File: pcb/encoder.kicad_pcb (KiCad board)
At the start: 2 copper layers, 32 x 57 mm, 2 parts, among them SW1 RKJXT1F42001, U1 Xiao2040

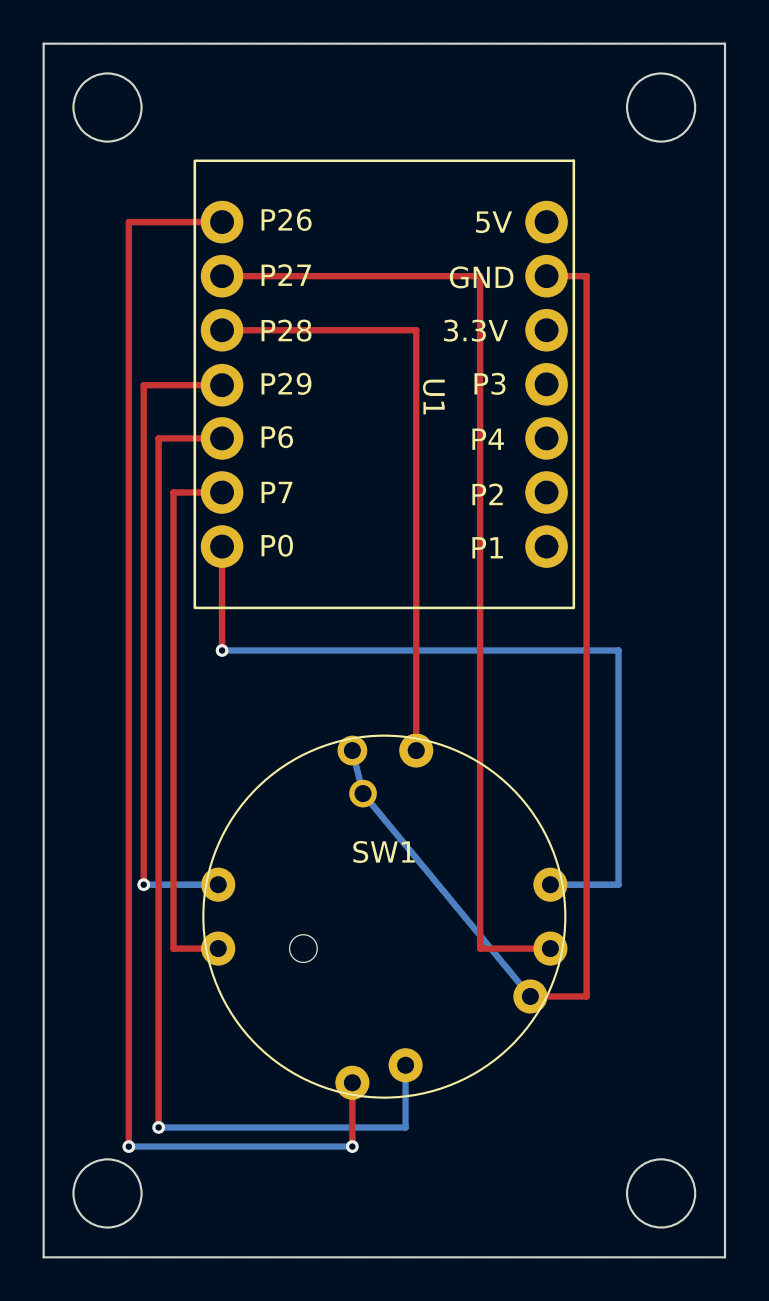
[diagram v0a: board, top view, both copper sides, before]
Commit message: Update PCB to bottom-layer-only routing constraints
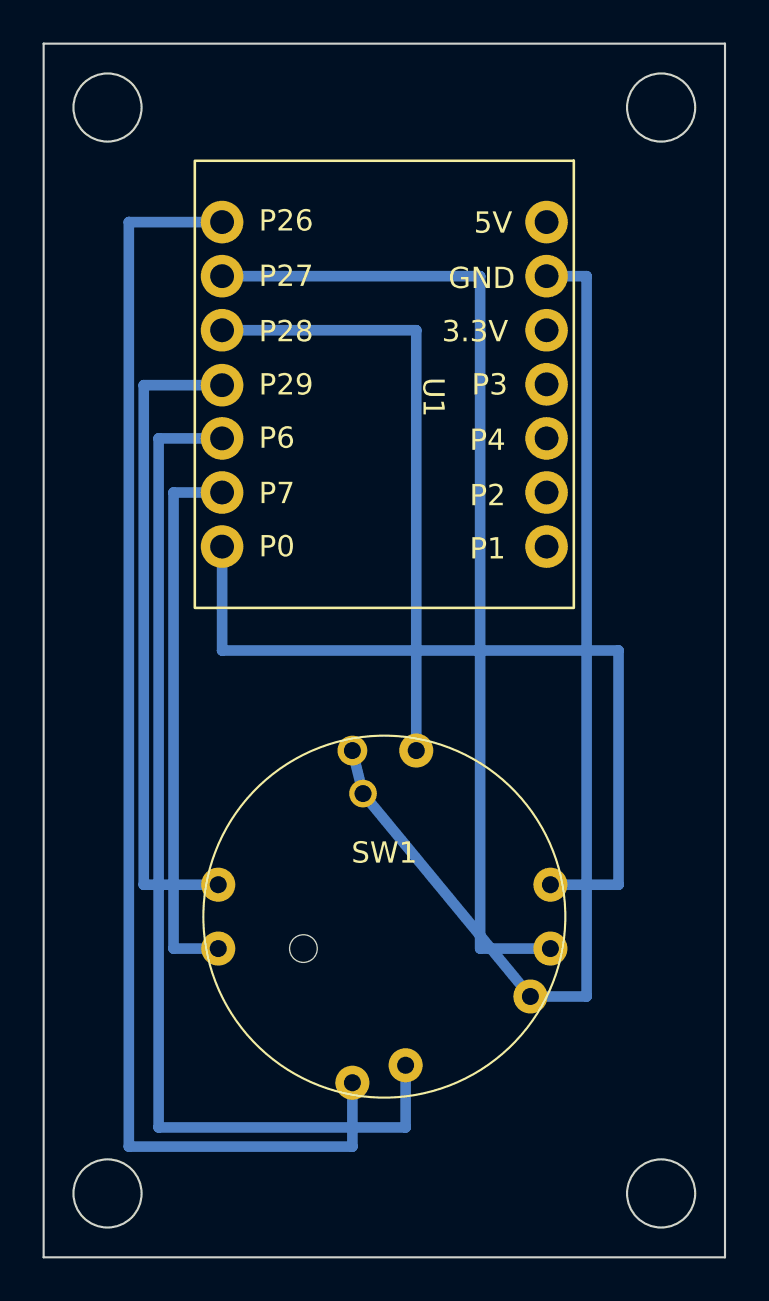
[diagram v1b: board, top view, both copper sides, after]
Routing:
- net SW_PUSH: vias 1 -> 0
- net SW_D: vias 1 -> 0
- net SW_A: vias 2 -> 0
- net ENC_B: vias 1 -> 0
- removed copper zone on B.Cu, net GND
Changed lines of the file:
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@@
 		(start 109.5 103.75)
 		(end 106.86 103.75)
-		(width 0.3)
-		(layer "F.Cu")
+		(width 0.5)
+		(layer "B.Cu")
 		(net "GND")
 	)
@@
 		(start 109.5 69.92)
 		(end 109.5 103.75)
-		(width 0.3)
-		(layer "F.Cu")
+		(width 0.5)
+		(layer "B.Cu")
 		(net "GND")
 	)
@@
 		(start 107.62 69.92)
 		(end 109.5 69.92)
-		(width 0.3)
-		(layer "F.Cu")
+		(width 0.5)
+		(layer "B.Cu")
 		(net "GND")
 	)
@@
 		(start 99 94.22)
 		(end 98.5 92.2)
-		(width 0.3)
+		(width 0.5)
 		(layer "B.Cu")
 		(net "GND")
@@
 		(start 106.86 103.75)
 		(end 99 94.22)
-		(width 0.3)
+		(width 0.5)
 		(layer "B.Cu")
 		(net "GND")
@@
 		(start 88 67.38)
 		(end 88 110.8)
-		(width 0.3)
-		(layer "F.Cu")
+		(width 0.5)
+		(layer "B.Cu")
 		(net "SW_A")
 	)
@@
 		(start 92.38 67.38)
 		(end 88 67.38)
-		(width 0.3)
-		(layer "F.Cu")
+		(width 0.5)
+		(layer "B.Cu")
 		(net "SW_A")
 	)
@@
 		(start 98.5 110.8)
 		(end 98.5 107.8)
-		(width 0.3)
-		(layer "F.Cu")
-		(net "SW_A")
-	)
-	(via
-		(at 88 110.8)
-		(size 0.6)
-		(drill 0.3)
-		(layers "F.Cu" "B.Cu")
-		(net "SW_A")
-	)
-	(via
-		(at 98.5 110.8)
-		(size 0.6)
-		(drill 0.3)
-		(layers "F.Cu" "B.Cu")
+		(width 0.5)
+		(layer "B.Cu")
 		(net "SW_A")
 	)
@@
 		(start 88 110.8)
 		(end 98.5 110.8)
-		(width 0.3)
+		(width 0.5)
 		(layer "B.Cu")
 		(net "SW_A")
@@
 		(start 92.38 69.92)
 		(end 104.5 69.92)
-		(width 0.3)
-		(layer "F.Cu")
+		(width 0.5)
+		(layer "B.Cu")
 		(net "SW_B")
 	)
@@
 		(start 104.5 101.5)
 		(end 107.8 101.5)
-		(width 0.3)
-		(layer "F.Cu")
+		(width 0.5)
+		(layer "B.Cu")
 		(net "SW_B")
 	)
@@
 		(start 104.5 69.92)
 		(end 104.5 101.5)
-		(width 0.3)
-		(layer "F.Cu")
+		(width 0.5)
+		(layer "B.Cu")
 		(net "SW_B")
 	)
@@
 		(start 92.38 72.46)
 		(end 101.5 72.46)
-		(width 0.3)
-		(layer "F.Cu")
+		(width 0.5)
+		(layer "B.Cu")
 		(net "SW_C")
 	)
@@
 		(start 101.5 72.46)
 		(end 101.5 92.2)
-		(width 0.3)
-		(layer "F.Cu")
+		(width 0.5)
+		(layer "B.Cu")
 		(net "SW_C")
 	)
@@
 		(start 92.38 75.04)
 		(end 88.7 75.04)
-		(width 0.3)
-		(layer "F.Cu")
+		(width 0.5)
+		(layer "B.Cu")
 		(net "SW_D")
 	)
@@
 		(start 88.7 75.04)
 		(end 88.7 98.5)
-		(width 0.3)
-		(layer "F.Cu")
-		(net "SW_D")
-	)
-	(via
-		(at 88.7 98.5)
-		(size 0.6)
-		(drill 0.3)
-		(layers "F.Cu" "B.Cu")
+		(width 0.5)
+		(layer "B.Cu")
 		(net "SW_D")
 	)
@@
 		(start 88.7 98.5)
 		(end 92.2 98.5)
-		(width 0.3)
+		(width 0.5)
 		(layer "B.Cu")
 		(net "SW_D")
@@
 		(start 89.4 77.54)
 		(end 89.4 109.9)
-		(width 0.3)
-		(layer "F.Cu")
+		(width 0.5)
+		(layer "B.Cu")
 		(net "SW_PUSH")
 	)
@@
 		(start 92.38 77.54)
 		(end 89.4 77.54)
-		(width 0.3)
-		(layer "F.Cu")
-		(net "SW_PUSH")
-	)
-	(via
-		(at 89.4 109.9)
-		(size 0.6)
-		(drill 0.3)
-		(layers "F.Cu" "B.Cu")
+		(width 0.5)
+		(layer "B.Cu")
 		(net "SW_PUSH")
 	)
@@
 		(start 101 109.9)
 		(end 101 106.98)
-		(width 0.3)
+		(width 0.5)
 		(layer "B.Cu")
 		(net "SW_PUSH")
@@
 		(start 89.4 109.9)
 		(end 101 109.9)
-		(width 0.3)
+		(width 0.5)
 		(layer "B.Cu")
 		(net "SW_PUSH")
@@
 		(start 92.38 80.08)
 		(end 90.1 80.08)
-		(width 0.3)
-		(layer "F.Cu")
+		(width 0.5)
+		(layer "B.Cu")
 		(net "ENC_A")
 	)
@@
 		(start 90.1 80.08)
 		(end 90.1 101.5)
-		(width 0.3)
-		(layer "F.Cu")
+		(width 0.5)
+		(layer "B.Cu")
 		(net "ENC_A")
 	)
@@
 		(start 90.1 101.5)
 		(end 92.2 101.5)
-		(width 0.3)
-		(layer "F.Cu")
+		(width 0.5)
+		(layer "B.Cu")
 		(net "ENC_A")
 	)
@@
 		(start 92.38 82.62)
 		(end 92.38 87.5)
-		(width 0.3)
-		(layer "F.Cu")
-		(net "ENC_B")
-	)
-	(via
-		(at 92.38 87.5)
-		(size 0.6)
-		(drill 0.3)
-		(layers "F.Cu" "B.Cu")
+		(width 0.5)
+		(layer "B.Cu")
 		(net "ENC_B")
 	)
@@
 		(start 92.38 87.5)
 		(end 111 87.5)
-		(width 0.3)
+		(width 0.5)
 		(layer "B.Cu")
 		(net "ENC_B")
@@
 		(start 111 87.5)
 		(end 111 98.5)
-		(width 0.3)
+		(width 0.5)
 		(layer "B.Cu")
 		(net "ENC_B")
@@
 		(start 111 98.5)
 		(end 107.8 98.5)
-		(width 0.3)
+		(width 0.5)
 		(layer "B.Cu")
 		(net "ENC_B")
 	)
-	(zone
-		(net "GND")
-		(layer "B.Cu")
-		(hatch edge 0.5)
-		(connect_pads
-			(clearance 0.3)
-		)
-		(min_thickness 0.25)
-		(fill yes
-			(thermal_gap 0.5)
-			(thermal_bridge_width 0.5)
-			(island_removal_mode 0)
-		)
-		(polygon
-			(pts
-				(xy 84 59) (xy 116 59) (xy 116 116) (xy 84 116)
-			)
-		)
-	)
 	(embedded_fonts no)
